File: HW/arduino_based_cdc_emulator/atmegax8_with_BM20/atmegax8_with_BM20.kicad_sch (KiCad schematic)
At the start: 66 parts, among them IC1 ATMEGA328PB-AU, J1 TEST_FLASH_MODE, P1 CONN_10, P2 SPI, U1 78L05-RESCUE-atmegax8_with_BM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, U2 BM20, U3 LM358, Y1 Crystal_GND24

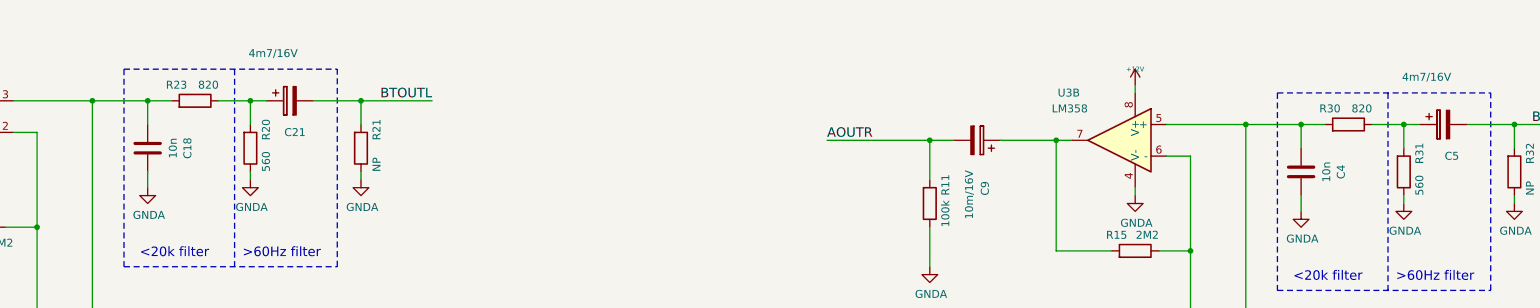
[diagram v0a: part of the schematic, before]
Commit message: disabled input filters,for now
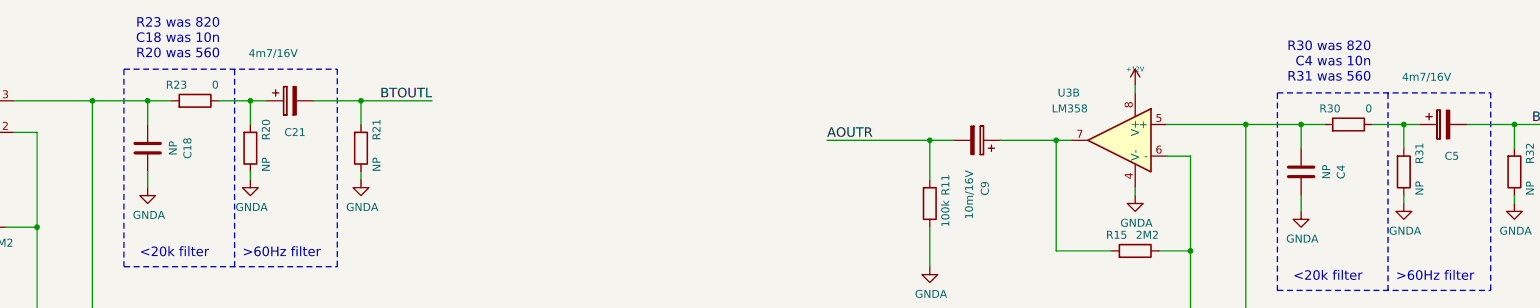
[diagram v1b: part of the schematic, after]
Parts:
- C18, C4: value 10n -> NP
- R20, R31: value 560 -> NP
- R23, R30: value 820 -> 0
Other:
- note added: "R23 was 820 C18 was 10n R20 was 560"
- note added: "R30 was 820 C4 was 10n R31 was 560"
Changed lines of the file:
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@@
     (effects (font (size 1.524 1.524)) (justify left bottom))
+  )
+  (text "R23 was 820\nC18 was 10n\nR20 was 560" (at 147.5232 32.7914 180)
+    (effects (font (size 1.524 1.524)) (justify right bottom))
   )
   (text ">60Hz filter" (at 151.13 64.77 0)
@@
   (text "<20k filter" (at 320.04 68.58 0)
     (effects (font (size 1.524 1.524)) (justify left bottom))
+  )
+  (text "R30 was 820\nC4 was 10n\nR31 was 560" (at 332.5876 36.5506 180)
+    (effects (font (size 1.524 1.524)) (justify right bottom))
   )
   (text ">60Hz filter" (at 336.55 68.58 0)
@@
       (effects (font (size 1.27 1.27)) (justify right))
     )
-    (property "Value" "820" (id 1) (at 147.32 36.83 90)
+    (property "Value" "0" (id 1) (at 147.32 36.83 90)
       (effects (font (size 1.27 1.27)) (justify right))
     )
@@
       (effects (font (size 1.27 1.27)) (justify right))
     )
-    (property "Value" "560" (id 1) (at 154.94 50.8 90)
+    (property "Value" "NP" (id 1) (at 154.94 50.8 90)
       (effects (font (size 1.27 1.27)) (justify right))
     )
@@
       (effects (font (size 1.27 1.27)) (justify right))
     )
-    (property "Value" "820" (id 1) (at 332.74 40.64 90)
+    (property "Value" "0" (id 1) (at 332.74 40.64 90)
       (effects (font (size 1.27 1.27)) (justify right))
     )
@@
       (effects (font (size 1.27 1.27)) (justify right))
     )
-    (property "Value" "560" (id 1) (at 340.36 54.61 90)
+    (property "Value" "NP" (id 1) (at 340.36 54.61 90)
       (effects (font (size 1.27 1.27)) (justify right))
     )
@@
     (in_bom yes)
     (property "Reference" "C18" (id 0) (at 142.3162 46.99 90))
-    (property "Value" "10n" (id 1) (at 139.9794 46.99 90))
+    (property "Value" "NP" (id 1) (at 139.979 46.99 90))
     (property "Footprint" "Capacitors_SMD.pretty:C_0805_HandSoldering" (id 2) (at 135.89 46.99 0)
       (effects (font (size 1.524 1.524)) hide)
@@
     (in_bom yes)
     (property "Reference" "C4" (id 0) (at 327.7362 50.8 90))
-    (property "Value" "10n" (id 1) (at 325.3994 50.8 90))
+    (property "Value" "NP" (id 1) (at 325.399 50.8 90))
     (property "Footprint" "Capacitors_SMD.pretty:C_0805_HandSoldering" (id 2) (at 321.31 50.8 0)
       (effects (font (size 1.524 1.524)) hide)
